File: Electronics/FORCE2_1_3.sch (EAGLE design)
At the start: 17 parts, among them J4 PTH, SW1 22-23-2031, SW2 22-23-2031, X1 22-23-2051, X2 22-23-2051, X3 22-23-2021

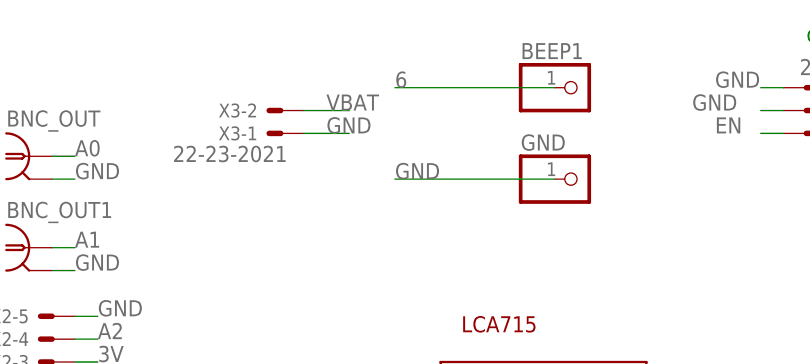
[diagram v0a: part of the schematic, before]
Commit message: First commit. Added electronics, stl file, and readme
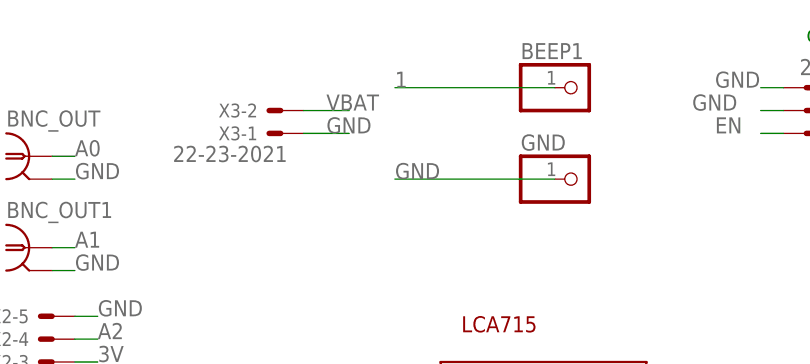
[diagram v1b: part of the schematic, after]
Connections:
- net 1: now also BEEP1.1
- net 6: no longer BEEP1.1
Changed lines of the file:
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@@
 <grid distance="0.1" unitdist="inch" unit="inch" style="lines" multiple="1" display="yes" altdistance="0.01" altunitdist="inch" altunit="inch"/>
 <layers>
-<layer number="1" name="Top" color="4" fill="1" visible="no" active="no"/>
-<layer number="2" name="Route2" color="16" fill="1" visible="no" active="no"/>
-<layer number="3" name="Route3" color="17" fill="1" visible="no" active="no"/>
-<layer number="4" name="Route4" color="18" fill="1" visible="no" active="no"/>
-<layer number="5" name="Route5" color="19" fill="1" visible="no" active="no"/>
-<layer number="6" name="Route6" color="25" fill="1" visible="no" active="no"/>
-<layer number="7" name="Route7" color="26" fill="1" visible="no" active="no"/>
-<layer number="8" name="Route8" color="27" fill="1" visible="no" active="no"/>
-<layer number="9" name="Route9" color="28" fill="1" visible="no" active="no"/>
-<layer number="10" name="Route10" color="29" fill="1" visible="no" active="no"/>
-<layer number="11" name="Route11" color="30" fill="1" visible="no" active="no"/>
-<layer number="12" name="Route12" color="20" fill="1" visible="no" active="no"/>
-<layer number="13" name="Route13" color="21" fill="1" visible="no" active="no"/>
-<layer number="14" name="Route14" color="22" fill="1" visible="no" active="no"/>
-<layer number="15" name="Route15" color="23" fill="1" visible="no" active="no"/>
-<layer number="16" name="Bottom" color="1" fill="1" visible="no" active="no"/>
-<layer number="17" name="Pads" color="2" fill="1" visible="no" active="no"/>
-<layer number="18" name="Vias" color="2" fill="1" visible="no" active="no"/>
-<layer number="19" name="Unrouted" color="6" fill="1" visible="no" active="no"/>
-<layer number="20" name="Dimension" color="24" fill="1" visible="no" active="no"/>
-<layer number="21" name="tPlace" color="7" fill="1" visible="no" active="no"/>
-<layer number="22" name="bPlace" color="7" fill="1" visible="no" active="no"/>
-<layer number="23" name="tOrigins" color="15" fill="1" visible="no" active="no"/>
-<layer number="24" name="bOrigins" color="15" fill="1" visible="no" active="no"/>
-<layer number="25" name="tNames" color="7" fill="1" visible="no" active="no"/>
-<layer number="26" name="bNames" color="7" fill="1" visible="no" active="no"/>
-<layer number="27" name="tValues" color="7" fill="1" visible="no" active="no"/>
-<layer number="28" name="bValues" color="7" fill="1" visible="no" active="no"/>
+<layer number="1" name="Top" color="4" fill="1" visible="yes" active="no"/>
+<layer number="2" name="Route2" color="16" fill="1" visible="yes" active="no"/>
+<layer number="3" name="Route3" color="17" fill="1" visible="yes" active="no"/>
+<layer number="4" name="Route4" color="18" fill="1" visible="yes" active="no"/>
+<layer number="5" name="Route5" color="19" fill="1" visible="yes" active="no"/>
+<layer number="6" name="Route6" color="25" fill="1" visible="yes" active="no"/>
+<layer number="7" name="Route7" color="26" fill="1" visible="yes" active="no"/>
+<layer number="8" name="Route8" color="27" fill="1" visible="yes" active="no"/>
+<layer number="9" name="Route9" color="28" fill="1" visible="yes" active="no"/>
+<layer number="10" name="Route10" color="29" fill="1" visible="yes" active="no"/>
+<layer number="11" name="Route11" color="30" fill="1" visible="yes" active="no"/>
+<layer number="12" name="Route12" color="20" fill="1" visible="yes" active="no"/>
+<layer number="13" name="Route13" color="21" fill="1" visible="yes" active="no"/>
+<layer number="14" name="Route14" color="22" fill="1" visible="yes" active="no"/>
+<layer number="15" name="Route15" color="23" fill="1" visible="yes" active="no"/>
+<layer number="16" name="Bottom" color="1" fill="1" visible="yes" active="no"/>
+<layer number="17" name="Pads" color="2" fill="1" visible="yes" active="no"/>
+<layer number="18" name="Vias" color="2" fill="1" visible="yes" active="no"/>
+<layer number="19" name="Unrouted" color="6" fill="1" visible="yes" active="no"/>
+<layer number="20" name="Dimension" color="24" fill="1" visible="yes" active="no"/>
+<layer number="21" name="tPlace" color="7" fill="1" visible="yes" active="no"/>
+<layer number="22" name="bPlace" color="7" fill="1" visible="yes" active="no"/>
+<layer number="23" name="tOrigins" color="15" fill="1" visible="yes" active="no"/>
+<layer number="24" name="bOrigins" color="15" fill="1" visible="yes" active="no"/>
+<layer number="25" name="tNames" color="7" fill="1" visible="yes" active="no"/>
+<layer number="26" name="bNames" color="7" fill="1" visible="yes" active="no"/>
+<layer number="27" name="tValues" color="7" fill="1" visible="yes" active="no"/>
+<layer number="28" name="bValues" color="7" fill="1" visible="yes" active="no"/>
 <layer number="29" name="tStop" color="7" fill="3" visible="no" active="no"/>
 <layer number="30" name="bStop" color="7" fill="6" visible="no" active="no"/>
@@
 <layer number="35" name="tGlue" color="7" fill="4" visible="no" active="no"/>
 <layer number="36" name="bGlue" color="7" fill="5" visible="no" active="no"/>
-<layer number="37" name="tTest" color="7" fill="1" visible="no" active="no"/>
-<layer number="38" name="bTest" color="7" fill="1" visible="no" active="no"/>
+<layer number="37" name="tTest" color="7" fill="1" visible="yes" active="no"/>
+<layer number="38" name="bTest" color="7" fill="1" visible="yes" active="no"/>
 <layer number="39" name="tKeepout" color="4" fill="11" visible="no" active="no"/>
 <layer number="40" name="bKeepout" color="1" fill="11" visible="no" active="no"/>
@@
 <layer number="44" name="Drills" color="7" fill="1" visible="no" active="no"/>
 <layer number="45" name="Holes" color="7" fill="1" visible="no" active="no"/>
-<layer number="46" name="Milling" color="3" fill="1" visible="no" active="no"/>
-<layer number="47" name="Measures" color="7" fill="1" visible="no" active="no"/>
-<layer number="48" name="Document" color="7" fill="1" visible="no" active="no"/>
-<layer number="49" name="Reference" color="7" fill="1" visible="no" active="no"/>
-<layer number="50" name="dxf" color="7" fill="1" visible="no" active="no"/>
-<layer number="51" name="tDocu" color="7" fill="1" visible="no" active="no"/>
-<layer number="52" name="bDocu" color="7" fill="1" visible="no" active="no"/>
-<layer number="53" name="tGND_GNDA" color="7" fill="1" visible="no" active="no"/>
-<layer number="54" name="bGND_GNDA" color="7" fill="1" visible="no" active="no"/>
-<layer number="56" name="wert" color="7" fill="1" visible="no" active="no"/>
-<layer number="57" name="tCAD" color="7" fill="1" visible="no" active="no"/>
-<layer number="59" name="tCarbon" color="7" fill="1" visible="no" active="no"/>
-<layer number="60" name="bCarbon" color="7" fill="1" visible="no" active="no"/>
+<layer number="46" name="Milling" color="3" fill="1" visible="yes" active="no"/>
+<layer number="47" name="Measures" color="7" fill="1" visible="yes" active="no"/>
+<layer number="48" name="Document" color="7" fill="1" visible="yes" active="no"/>
+<layer number="49" name="Reference" color="7" fill="1" visible="yes" active="no"/>
+<layer number="50" name="dxf" color="7" fill="1" visible="yes" active="no"/>
+<layer number="51" name="tDocu" color="7" fill="1" visible="yes" active="no"/>
+<layer number="52" name="bDocu" color="7" fill="1" visible="yes" active="no"/>
+<layer number="53" name="tGND_GNDA" color="7" fill="1" visible="yes" active="no"/>
+<layer number="54" name="bGND_GNDA" color="7" fill="1" visible="yes" active="no"/>
+<layer number="56" name="wert" color="7" fill="1" visible="yes" active="no"/>
+<layer number="57" name="tCAD" color="7" fill="1" visible="yes" active="no"/>
+<layer number="59" name="tCarbon" color="7" fill="1" visible="yes" active="no"/>
+<layer number="60" name="bCarbon" color="7" fill="1" visible="yes" active="no"/>
 <layer number="88" name="SimResults" color="9" fill="1" visible="yes" active="yes"/>
 <layer number="89" name="SimProbes" color="9" fill="1" visible="yes" active="yes"/>
@@
 <label x="-208.28" y="-185.42" size="1.778" layer="95"/>
 </segment>
+<segment>
+<pinref part="BEEP1" gate="G$1" pin="1"/>
+<wire x1="-254" y1="-78.74" x2="-271.78" y2="-78.74" width="0.1524" layer="91"/>
+<label x="-271.78" y="-78.74" size="1.778" layer="95"/>
+</segment>
 </net>
 <net name="4" class="0">
@@
 </segment>
 <segment>
-<pinref part="BEEP1" gate="G$1" pin="1"/>
-<wire x1="-254" y1="-78.74" x2="-271.78" y2="-78.74" width="0.1524" layer="91"/>
-<label x="-271.78" y="-78.74" size="1.778" layer="95"/>
-</segment>
-<segment>
